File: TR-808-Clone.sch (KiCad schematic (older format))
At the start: 570 parts, among them J1 BD, J10 OH, J11 CH, J12 MASTER, J2 SD, J3 LT, J4 MT, J5 HT, J6 RS, J7 CP, J8 CB, J9 CY, P1 CONN_02X05, P2 CONN_01X08, Q10 MMBT3906, Q11 MMBT3904, Q12 MMBT3906, Q13 J111/J112, Q22 MMBT3904, Q27-1 MMBT3904, Q28 MMBT3904, Q29 MMBT3906, Q31 MMBT3904, Q32 MMBT3904, Q33 MMBT3904, Q34 MMBT3904, Q35 MMBT3904, Q39 MMBT3904, Q40 MMBT3906, Q41 MMBT3904, Q42 MMBT3904, Q43 MMBT3904, Q44 MMBT3904, Q45 MMBT3904, Q46 MMBT3906, Q47 MMBT3904, Q48 MMBT3904, Q49 MMBT3904, Q50 MMBT3904, Q51 MMBT3906, Q52 MMBT3904, Q53 MMBT3904, Q54 MMBT3906, Q55 MMBT3904, Q56 MMBT3904, Q57 MMBT3906, Q58 MMBT3904, Q59 MMBT3904, Q60 MMBT3906, Q61 MMBT3904, Q62 MMBT3904, Q63 MMBT3904, Q65 MMBT3906, Q66 MMBT3906, Q67 MMBT3904, Q68 MMBT3904, Q69 MMBT3904, Q70 MMBT3904, Q71/72 DMMT3906, Q73 MMBT3904, Q74 J111/J112, U10 CD4053, U11 CD4053, U12 4558, U13 4558, U14 4558, U15 4558, U16 4558, U17 4558, U18 4558, U19 4558, U20 4558, U21 4558, U22 LM13700, U23 LM339-, U24 4558, U25 CD4053, U26 CD4053, U4 4558, U6 CD4011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

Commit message: started version 2.0 schematic changes. Added missing R365, replaced LM13700 VCA with discrete BA662 from Open Music Labs, replaced clap and hi hat matched pairs with single NPN/PNP Qs
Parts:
- removed Q22: MMBT3904, MyModules:SOT23-132-JRL, symbol MMBT3904
- removed Q71/72: DMMT3906, MyModules:SOT363-JRL, symbol DMMT3906
- removed U22: LM13700, MyModules:SO16-JRL, symbol LM13700
- removed U8: CD4053, Housings_SSOP:TSSOP-16_4.4x5mm_Pitch0.65mm, symbol CD4053
- removed U9: 4558, MyModules:TSSOP8-JRL, symbol TL072-
- added Q36: MMBT3904, MyModules:SOT23-132-JRL, symbol MMBT3904
- added Q37, Q71, Q72: MMBT3906, MyModules:SOT23-132-JRL, symbol MMBT3906
- added R329: 4.7K, MyModules:SM0603-R-JRL, symbol R_US
- added R334: 10K, MyModules:SM0603-R-JRL, symbol R_US
- added R365: 82K, MyModules:SM0603-R-JRL, symbol R_US
- added TP8: TEST_POINT, MyModules:TEST_POINT_LOOP_4592, symbol TEST_POINT
- R34: value 10K -> 22K
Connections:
- net labels added: MA_TRIG
- net labels removed: CP_SW
- wire segments 1302 -> 1288
- no-connect marks 30 -> 20
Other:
- note removed: "LEVEL\nSHIFT"
- note removed: "LM13700 substituted for BA662\nSee also:\nhttp://electro-music.com/forum/phpbb-files/808_clap_156.png"
- note removed: "OR CONFIGURE SPARE OTA \nAS UNITY GAIN BUFFER"
- note removed: "PROBABLY SHOULD \nHAVE USED 2X 733\nPNP HERE INSTEAD"
- note removed: "WHY NOT USE A FET\nBUFFER HERE, YOU TWIT?!"
- moved on the sheet: C135, C150, D67, Q29, R345, R361, R374, R378, R383

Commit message: Sync LED control pins added, tom clipping diodes changed to BAT54 with series resistor
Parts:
- added R? (x3): 220, MyModules:SM0603-R-JRL, symbol R_US
- D80, D81, D82, D83: value 1N4148 -> BAT54; symbol D -> D_Schottky
- D84, D85: value 1N4148 -> BAT45; symbol D -> D_Schottky
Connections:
- net at D80.1 (K), D81.2 (A): now also R?.1; no longer VR11.1
- net at D82.1 (K), D83.2 (A): now also R?.1; no longer VR13.1
- net at D84.1 (K), D85.2 (A): now also R?.1; no longer VR15.1
- new net: R?.2, VR11.1
- new net: R?.2, VR13.1
- new net: R?.2, VR15.1
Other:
- note added: "http://rezzonics.blogspot.ca/2014/01/germanium-diodes-vs-schottky-diodes-for.html"
- note removed: "R365 (82K) to GND\nis missing here!"
- moved on the sheet: D80, D81, D82, D83, D84, D85, VR11, VR13, VR15

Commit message: updated BAT54 array schematic symobl and footprint
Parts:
- removed D80, D81, D82, D83: BAT54, MyModules:SOD323-C1A2, symbol D_Schottky
- removed D84, D85: BAT45, MyModules:SOD323-C1A2, symbol D_Schottky
- added D80, D82, D84: BAT54SL, symbol BAT54SL
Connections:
- net at C76.1, C78.2, R230.2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: now also D80.1 (A), D80.2 (K)
- net at R?.1: now also D80.3 (KA)
- net at C90.1, C92.2, R259.2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: now also D82.1 (A), D82.2 (K)
- net at R?.1: now also D82.3 (KA)
- net at C103.1, C105.2, R286.2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: now also D84.1 (A), D84.2 (K)
- net at R?.1: now also D84.3 (KA)
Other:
- moved on the sheet: R?, VR11, VR13, VR15

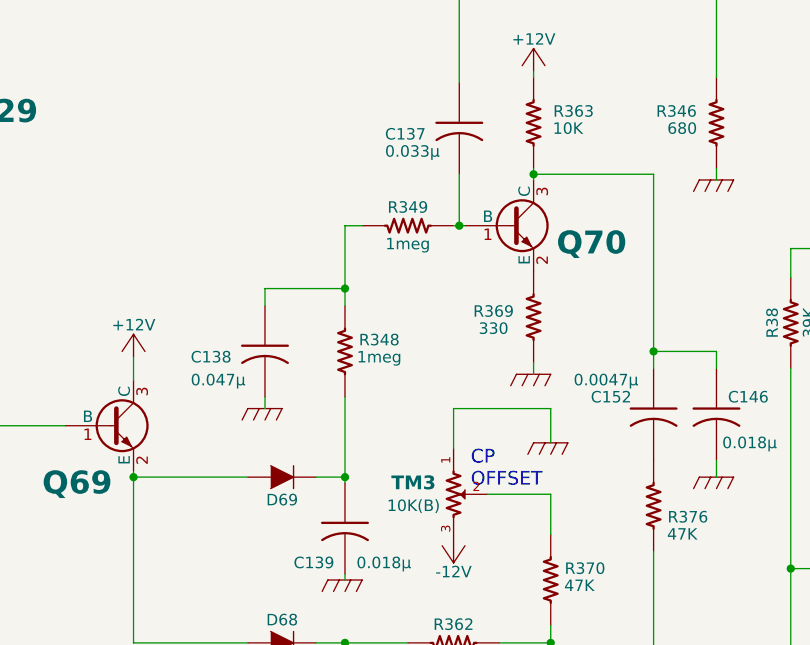
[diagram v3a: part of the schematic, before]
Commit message: major changes to PCB started, beginning with matching hardware positions with latest panel design from Inkscape
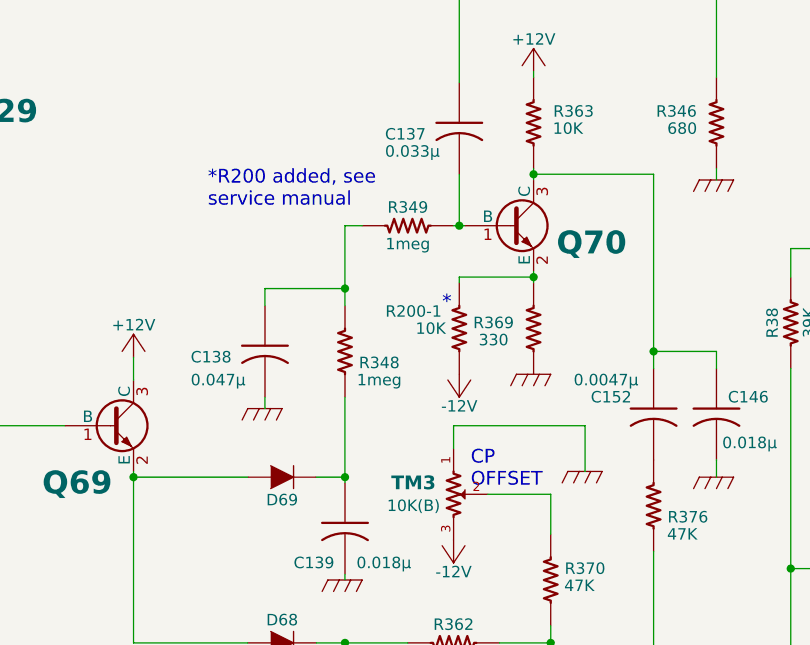
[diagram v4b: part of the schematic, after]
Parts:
- added R200-1: 10K, MyModules:SM0603-R-JRL, symbol R_US
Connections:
- net -12V: now also R200-1.2
- net at Q70.2 (E), R369.1: now also R200-1.1
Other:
- note added: "*R200 added, see \nservice manual"
- moved on the sheet: R369
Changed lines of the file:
@@
 U 1 1 56A37FD8
 P 4300 16100
-F 0 "R348" H 4450 16150 50  0000 C CNN
-F 1 "1meg" H 4450 16075 50  0000 C CNN
+F 0 "R348" H 4450 16050 50  0000 C CNN
+F 1 "1meg" H 4450 15975 50  0000 C CNN
 F 2 "MyModules:SM0603-R-JRL" H 4300 16100 60  0001 C CNN
 F 3 "" H 4300 16100 60  0000 C CNN
@@
 L GND_R #PWR0111
 U 1 1 56A4C0C1
-P 5200 16500
-F 0 "#PWR0111" H 5200 16500 30  0001 C CNN
-F 1 "GND_R" H 5200 16400 30  0001 C CNN
-F 2 "" H 5200 16500 60  0000 C CNN
-F 3 "" H 5200 16500 60  0000 C CNN
-	1    5200 16500
+P 5350 16625
+F 0 "#PWR0111" H 5350 16625 30  0001 C CNN
+F 1 "GND_R" H 5350 16525 30  0001 C CNN
+F 2 "" H 5350 16625 60  0000 C CNN
+F 3 "" H 5350 16625 60  0000 C CNN
+	1    5350 16625
 	1    0    0    -1
 $EndComp
@@
 L R_US R369
 U 1 1 56AC4C7C
-P 5125 15950
-F 0 "R369" H 4950 15975 50  0000 C CNN
-F 1 "330" H 4950 15900 50  0000 C CNN
-F 2 "MyModules:SM0603-R-JRL" H 5125 15950 60  0001 C CNN
-F 3 "" H 5125 15950 60  0000 C CNN
-	1    5125 15950
+P 5125 16000
+F 0 "R369" H 4950 16025 50  0000 C CNN
+F 1 "330" H 4950 15950 50  0000 C CNN
+F 2 "MyModules:SM0603-R-JRL" H 5125 16000 60  0001 C CNN
+F 3 "" H 5125 16000 60  0000 C CNN
+	1    5125 16000
 	1    0    0    -1
 $EndComp
@@
 Connection ~ 4800 15550
 Wire Wire Line
-	5200 16350 5200 16500
+	5350 16425 5350 16625
 Wire Wire Line
 	4925 16725 5200 16725
@@
 	5200 16725 5200 16900
 Wire Wire Line
-	4775 16525 4775 16350
+	4775 16525 4775 16425
 Wire Wire Line
-	4775 16350 5200 16350
+	4775 16425 5350 16425
 Wire Wire Line
 	5200 17300 5200 17375
@@
 	4375 15550 4300 15550
 Wire Wire Line
-	5125 16150 5125 16200
-Wire Wire Line
 	5125 15325 5650 15325
 Wire Wire Line
@@
 Wire Wire Line
 	33875 1550 33900 1550
+Wire Wire Line
+	5125 15750 5125 15775
+Wire Wire Line
+	5125 15775 5125 15800
+$Comp
+L R_US R200-1
+U 1 1 57D8B314
+P 4800 16000
+F 0 "R200-1" H 4600 16075 50  0000 C CNN
+F 1 "10K" H 4675 16000 50  0000 C CNN
+F 2 "MyModules:SM0603-R-JRL" H 4800 16000 60  0001 C CNN
+F 3 "" H 4800 16000 60  0000 C CNN
+	1    4800 16000
+	1    0    0    -1
+$EndComp
+$Comp
+L -12V #PWR?
+U 1 1 57D8DBE5
+P 4800 16200
+F 0 "#PWR?" H 4800 16050 50  0001 C CNN
+F 1 "-12V" H 4800 16340 50  0000 C CNN
+F 2 "" H 4800 16200 60  0000 C CNN
+F 3 "" H 4800 16200 60  0000 C CNN
+	1    4800 16200
+	-1   0    0    1
+$EndComp
+Wire Wire Line
+	5125 15775 4800 15775
+Wire Wire Line
+	4800 15775 4800 15800
+Connection ~ 5125 15775
+Text Notes 4725 15925 0    60   ~ 0
+*
+Text Notes 3700 15475 0    60   ~ 0
+*R200 added, see \nservice manual
 $EndSCHEMATC

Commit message: assigning footprints before importing updated netlist into pcbnew
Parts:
- D80, D82, D84: footprint (none) -> MyModules:SOT23-132-JRL
- TM3, TM4: footprint MyModules:Bourns_3362P -> MyModules:TC33X-2
- gave numbers to parts that had none: 3

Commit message: surface mount polarized capacitors replace through hole capaictors. Updated netlist not yet imported into pcbnew
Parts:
- C106, C107, C123, C124, C147, C148, C154, C155, C156, C157, C158, C159, C25, C26, C29-1, C34-1, C55, C89, C93, C94: footprint MyModules:2MM-POL-CAP -> Capacitors_SMD:c_elec_6.3x5.3
- C109, C21, C43, C68, C82, C95: footprint MyModules:2MM-POL-CAP -> Capacitors_SMD:c_elec_5x5.3
- C120, C126, C143, C144, C145, C162, C163, C17, C19, C200, C23-1, C24, C31-1, C47, C49, C50, C51, C7, C8: footprint MyModules:2MM-POL-CAP -> Capacitors_SMD:c_elec_4x5.3
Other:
- moved on the sheet: C106, C107, C123, C124, C147, C148, C154, C155, C156, C157, C158, C159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

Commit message: first commit since importing netlist with updated footprints. Bit of a mess now. Major reroute is in order
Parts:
- C106, C107, C123, C124, C147, C148, C154, C155, C156, C157, C158, C159, C25, C26, C29-1, C34-1, C55, C89, C93, C94: footprint Capacitors_SMD:c_elec_6.3x5.3 -> Capacitors_SMD:c_elec_5x5.3
- C145: footprint Capacitors_SMD:c_elec_4x5.3 -> Capacitors_SMD:c_elec_5x5.3
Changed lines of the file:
@@
 F 0 "C29-1" H 32150 8475 50  0000 L CNN
 F 1 "47μ" H 32150 8275 50  0000 L CNN
-F 2 "Capacitors_SMD:c_elec_6.3x5.3" H 32100 8375 60  0001 C CNN
+F 2 "Capacitors_SMD:c_elec_5x5.3" H 32100 8375 60  0001 C CNN
 F 3 "" H 32100 8375 60  0000 C CNN
 	1    32100 8375
@@
 F 0 "C55" H 3875 10100 50  0000 L CNN
 F 1 "47μ" H 3600 10100 50  0000 L CNN
-F 2 "Capacitors_SMD:c_elec_6.3x5.3" H 3800 10225 60  0001 C CNN
+F 2 "Capacitors_SMD:c_elec_5x5.3" H 3800 10225 60  0001 C CNN
 F 3 "" H 3800 10225 60  0000 C CNN
 	1    3800 10225
@@
 F 0 "C145" V 9225 20900 50  0000 L CNN
 F 1 "33μ" V 9300 21150 50  0000 L CNN
-F 2 "Capacitors_SMD:c_elec_4x5.3" H 9375 21000 60  0001 C CNN
+F 2 "Capacitors_SMD:c_elec_5x5.3" H 9375 21000 60  0001 C CNN
 F 3 "" H 9375 21000 60  0000 C CNN
 	1    9375 21000
@@
 F 0 "C25" H 28225 8000 50  0000 L CNN
 F 1 "47μ" H 28225 7925 50  0000 L CNN
-F 2 "Capacitors_SMD:c_elec_6.3x5.3" H 28500 8025 60  0001 C CNN
+F 2 "Capacitors_SMD:c_elec_5x5.3" H 28500 8025 60  0001 C CNN
 F 3 "" H 28500 8025 60  0000 C CNN
 	1    28500 8025
@@
 F 0 "C34-1" H 30000 8025 50  0000 L CNN
 F 1 "47μ" H 30000 7950 50  0000 L CNN
-F 2 "Capacitors_SMD:c_elec_6.3x5.3" H 29850 8025 60  0001 C CNN
+F 2 "Capacitors_SMD:c_elec_5x5.3" H 29850 8025 60  0001 C CNN
 F 3 "" H 29850 8025 60  0000 C CNN
 	1    29850 8025
@@
 F 0 "C93" H 12025 14850 50  0000 L CNN
 F 1 "47μ" H 12200 14850 50  0000 L CNN
-F 2 "Capacitors_SMD:c_elec_6.3x5.3" H 12175 14975 60  0001 C CNN
+F 2 "Capacitors_SMD:c_elec_5x5.3" H 12175 14975 60  0001 C CNN
 F 3 "" H 12175 14975 60  0000 C CNN
 	1    12175 14975
@@
 F 0 "C26" H 11575 14850 50  0000 L CNN
 F 1 "47μ" H 11750 14850 50  0000 L CNN
-F 2 "Capacitors_SMD:c_elec_6.3x5.3" H 11725 14975 60  0001 C CNN
+F 2 "Capacitors_SMD:c_elec_5x5.3" H 11725 14975 60  0001 C CNN
 F 3 "" H 11725 14975 60  0000 C CNN
 	1    11725 14975
@@
 F 0 "C123" H 12875 14850 50  0000 L CNN
 F 1 "47μ" H 13050 14850 50  0000 L CNN
-F 2 "Capacitors_SMD:c_elec_6.3x5.3" H 13025 14975 60  0001 C CNN
+F 2 "Capacitors_SMD:c_elec_5x5.3" H 13025 14975 60  0001 C CNN
 F 3 "" H 13025 14975 60  0000 C CNN
 	1    13025 14975
@@
 F 0 "C106" H 12475 14850 50  0000 L CNN
 F 1 "47μ" H 12650 14850 50  0000 L CNN
-F 2 "Capacitors_SMD:c_elec_6.3x5.3" H 12625 14975 60  0001 C CNN
+F 2 "Capacitors_SMD:c_elec_5x5.3" H 12625 14975 60  0001 C CNN
 F 3 "" H 12625 14975 60  0000 C CNN
 	1    12625 14975
@@
 F 0 "C94" H 12025 15875 50  0000 L CNN
 F 1 "47μ" H 12200 15875 50  0000 L CNN
-F 2 "Capacitors_SMD:c_elec_6.3x5.3" H 12175 16000 60  0001 C CNN
+F 2 "Capacitors_SMD:c_elec_5x5.3" H 12175 16000 60  0001 C CNN
 F 3 "" H 12175 16000 60  0000 C CNN
 	1    12175 16000
@@
 F 0 "C89" H 11575 15875 50  0000 L CNN
 F 1 "47μ" H 11750 15875 50  0000 L CNN
-F 2 "Capacitors_SMD:c_elec_6.3x5.3" H 11725 16000 60  0001 C CNN
+F 2 "Capacitors_SMD:c_elec_5x5.3" H 11725 16000 60  0001 C CNN
 F 3 "" H 11725 16000 60  0000 C CNN
 	1    11725 16000
@@
 F 0 "C124" H 12875 15875 50  0000 L CNN
 F 1 "47μ" H 13050 15875 50  0000 L CNN
-F 2 "Capacitors_SMD:c_elec_6.3x5.3" H 13025 16000 60  0001 C CNN
+F 2 "Capacitors_SMD:c_elec_5x5.3" H 13025 16000 60  0001 C CNN
 F 3 "" H 13025 16000 60  0000 C CNN
 	1    13025 16000
@@
 F 0 "C107" H 12475 15875 50  0000 L CNN
 F 1 "47μ" H 12650 15875 50  0000 L CNN
-F 2 "Capacitors_SMD:c_elec_6.3x5.3" H 12625 16000 60  0001 C CNN
+F 2 "Capacitors_SMD:c_elec_5x5.3" H 12625 16000 60  0001 C CNN
 F 3 "" H 12625 16000 60  0000 C CNN
 	1    12625 16000
@@
 F 0 "C154" H 13800 14850 50  0000 L CNN
 F 1 "47μ" H 13975 14850 50  0000 L CNN
-F 2 "Capacitors_SMD:c_elec_6.3x5.3" H 13950 14975 60  0001 C CNN
+F 2 "Capacitors_SMD:c_elec_5x5.3" H 13950 14975 60  0001 C CNN
 F 3 "" H 13950 14975 60  0000 C CNN
 	1    13950 14975
@@
 F 0 "C147" H 13350 14850 50  0000 L CNN
 F 1 "47μ" H 13525 14850 50  0000 L CNN
-F 2 "Capacitors_SMD:c_elec_6.3x5.3" H 13500 14975 60  0001 C CNN
+F 2 "Capacitors_SMD:c_elec_5x5.3" H 13500 14975 60  0001 C CNN
 F 3 "" H 13500 14975 60  0000 C CNN
 	1    13500 14975
@@
 F 0 "C158" H 14650 14850 50  0000 L CNN
 F 1 "47μ" H 14825 14850 50  0000 L CNN
-F 2 "Capacitors_SMD:c_elec_6.3x5.3" H 14800 14975 60  0001 C CNN
+F 2 "Capacitors_SMD:c_elec_5x5.3" H 14800 14975 60  0001 C CNN
 F 3 "" H 14800 14975 60  0000 C CNN
 	1    14800 14975
@@
 F 0 "C156" H 14250 14850 50  0000 L CNN
 F 1 "47μ" H 14425 14850 50  0000 L CNN
-F 2 "Capacitors_SMD:c_elec_6.3x5.3" H 14400 14975 60  0001 C CNN
+F 2 "Capacitors_SMD:c_elec_5x5.3" H 14400 14975 60  0001 C CNN
 F 3 "" H 14400 14975 60  0000 C CNN
 	1    14400 14975
@@
 F 0 "C155" H 13800 15875 50  0000 L CNN
 F 1 "47μ" H 13975 15875 50  0000 L CNN
-F 2 "Capacitors_SMD:c_elec_6.3x5.3" H 13950 16000 60  0001 C CNN
+F 2 "Capacitors_SMD:c_elec_5x5.3" H 13950 16000 60  0001 C CNN
 F 3 "" H 13950 16000 60  0000 C CNN
 	1    13950 16000
@@
 F 0 "C148" H 13350 15875 50  0000 L CNN
 F 1 "47μ" H 13525 15875 50  0000 L CNN
-F 2 "Capacitors_SMD:c_elec_6.3x5.3" H 13500 16000 60  0001 C CNN
+F 2 "Capacitors_SMD:c_elec_5x5.3" H 13500 16000 60  0001 C CNN
 F 3 "" H 13500 16000 60  0000 C CNN
 	1    13500 16000
@@
 F 0 "C159" H 14650 15875 50  0000 L CNN
 F 1 "47μ" H 14825 15875 50  0000 L CNN
-F 2 "Capacitors_SMD:c_elec_6.3x5.3" H 14800 16000 60  0001 C CNN
+F 2 "Capacitors_SMD:c_elec_5x5.3" H 14800 16000 60  0001 C CNN
 F 3 "" H 14800 16000 60  0000 C CNN
 	1    14800 16000
@@
 F 0 "C157" H 14250 15875 50  0000 L CNN
 F 1 "47μ" H 14425 15875 50  0000 L CNN
-F 2 "Capacitors_SMD:c_elec_6.3x5.3" H 14400 16000 60  0001 C CNN
+F 2 "Capacitors_SMD:c_elec_5x5.3" H 14400 16000 60  0001 C CNN
 F 3 "" H 14400 16000 60  0000 C CNN
 	1    14400 16000

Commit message: epic pcb overhaul for 2.0 has begun. depressing
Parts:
- removed TP1, TP12, TP2, TP21, TP3, TP4, TP5, TP8: TEST_POINT, MyModules:TEST_POINT_LOOP_4592, symbol TEST_POINT
